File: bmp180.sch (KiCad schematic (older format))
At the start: 3 parts, among them U6 BMP180

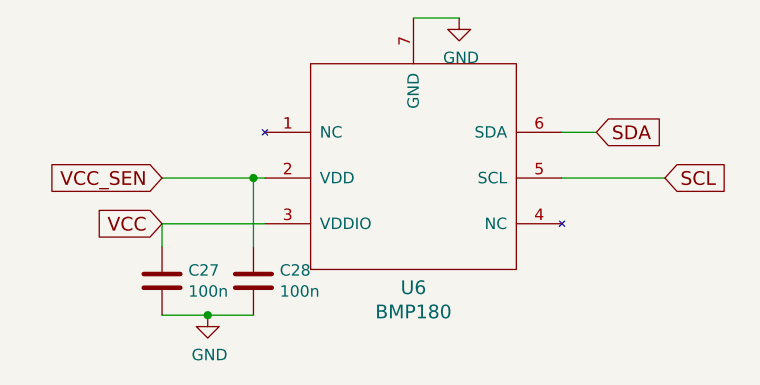
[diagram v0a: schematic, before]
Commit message: changed some netnames
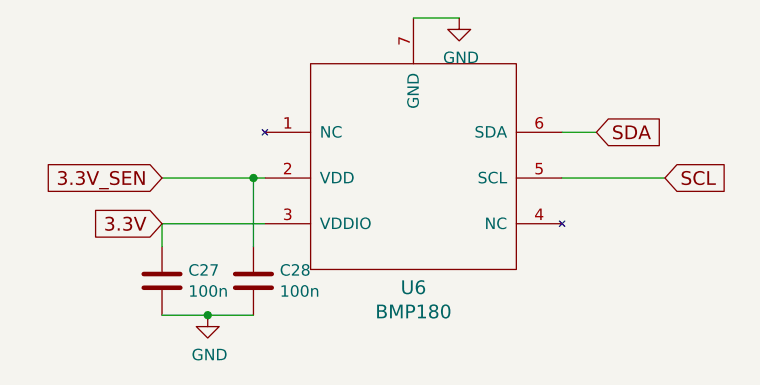
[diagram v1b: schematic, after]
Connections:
- net VCC renamed 3.3V
- net VCC_SEN renamed 3.3V_SEN
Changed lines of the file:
@@
 SCL
 Text GLabel 4500 4100 0    60   Input ~ 0
-VCC
+3.3V
 Wire Wire Line
 	4500 4100 4500 4200
 Text GLabel 4500 3900 0    60   Input ~ 0
-VCC_SEN
+3.3V_SEN
 $EndSCHEMATC
